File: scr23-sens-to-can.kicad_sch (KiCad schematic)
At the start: 61 parts, among them IC1 ADS1256IDBRG4, J1 ATM13-12PA-BM01, J2 6473711-1, J3 Conn_ST_STDC14, SW1 SW_SPDT, U1 SRV05-4, U10 AP63205WU, U2 SRV05-4, U4 TJA1042T-3, U5 AP7370-33Y-13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

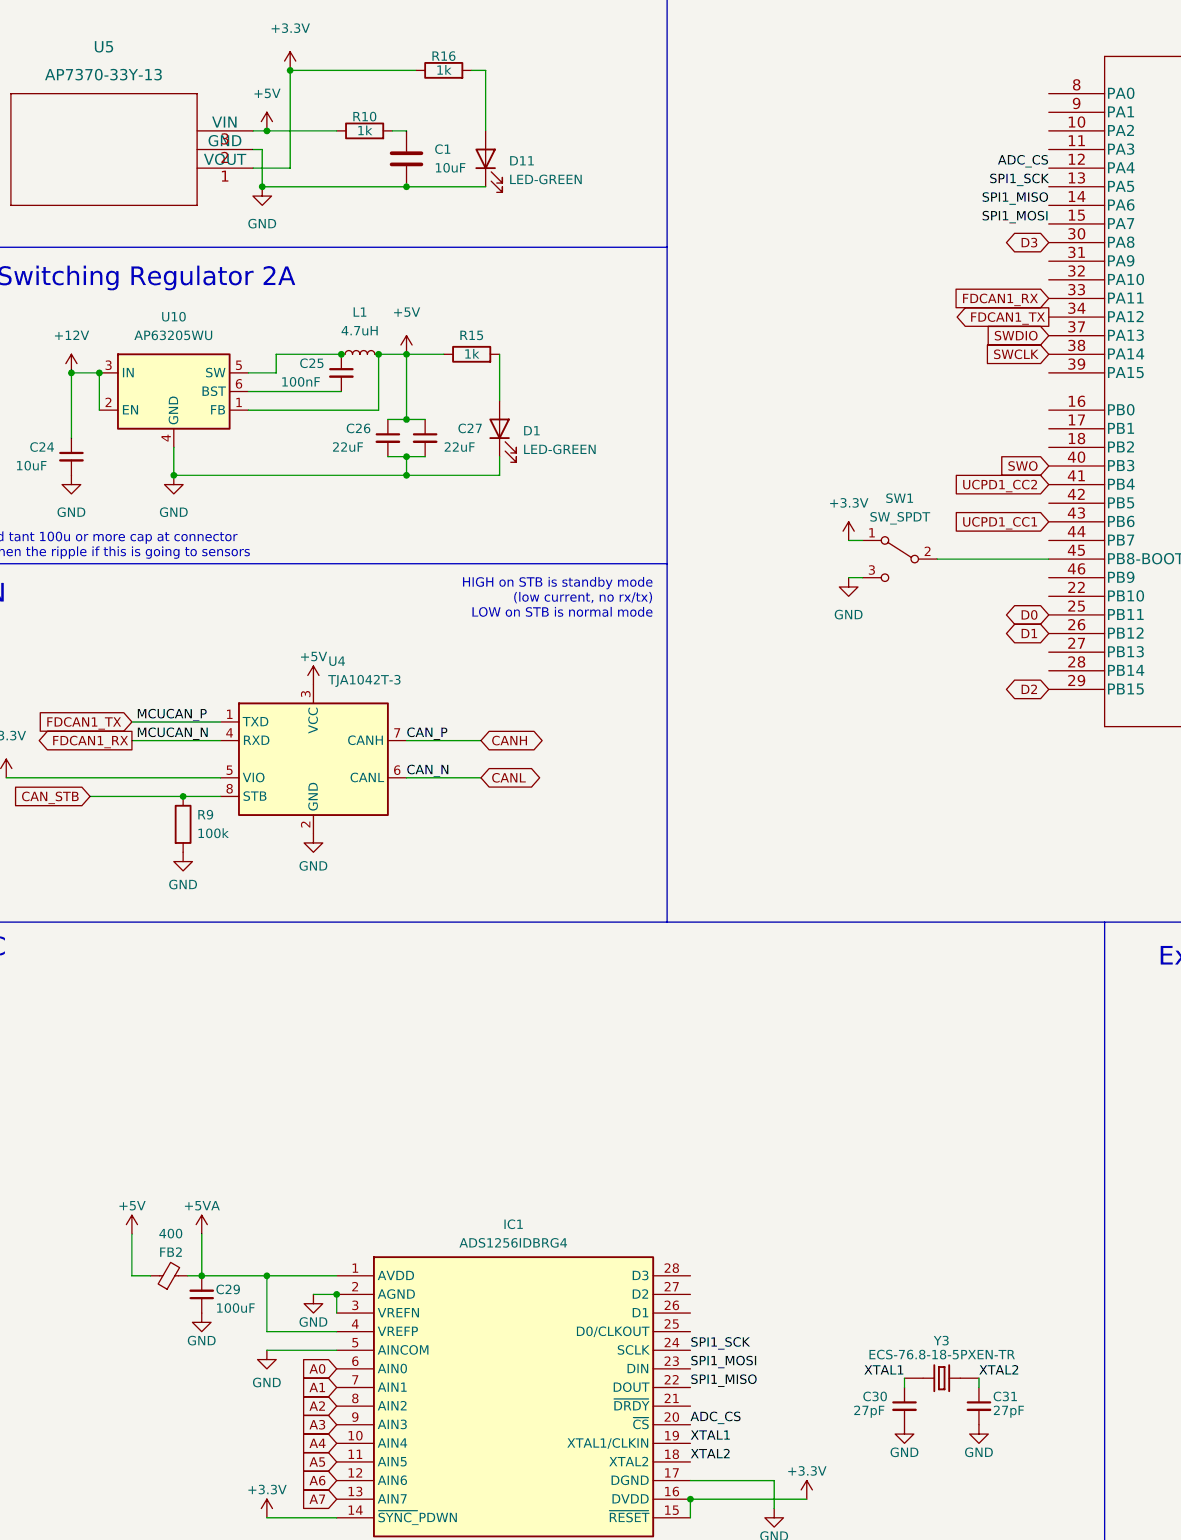
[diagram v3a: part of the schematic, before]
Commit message: add voltage reference, might need to change switching regulator cap packages
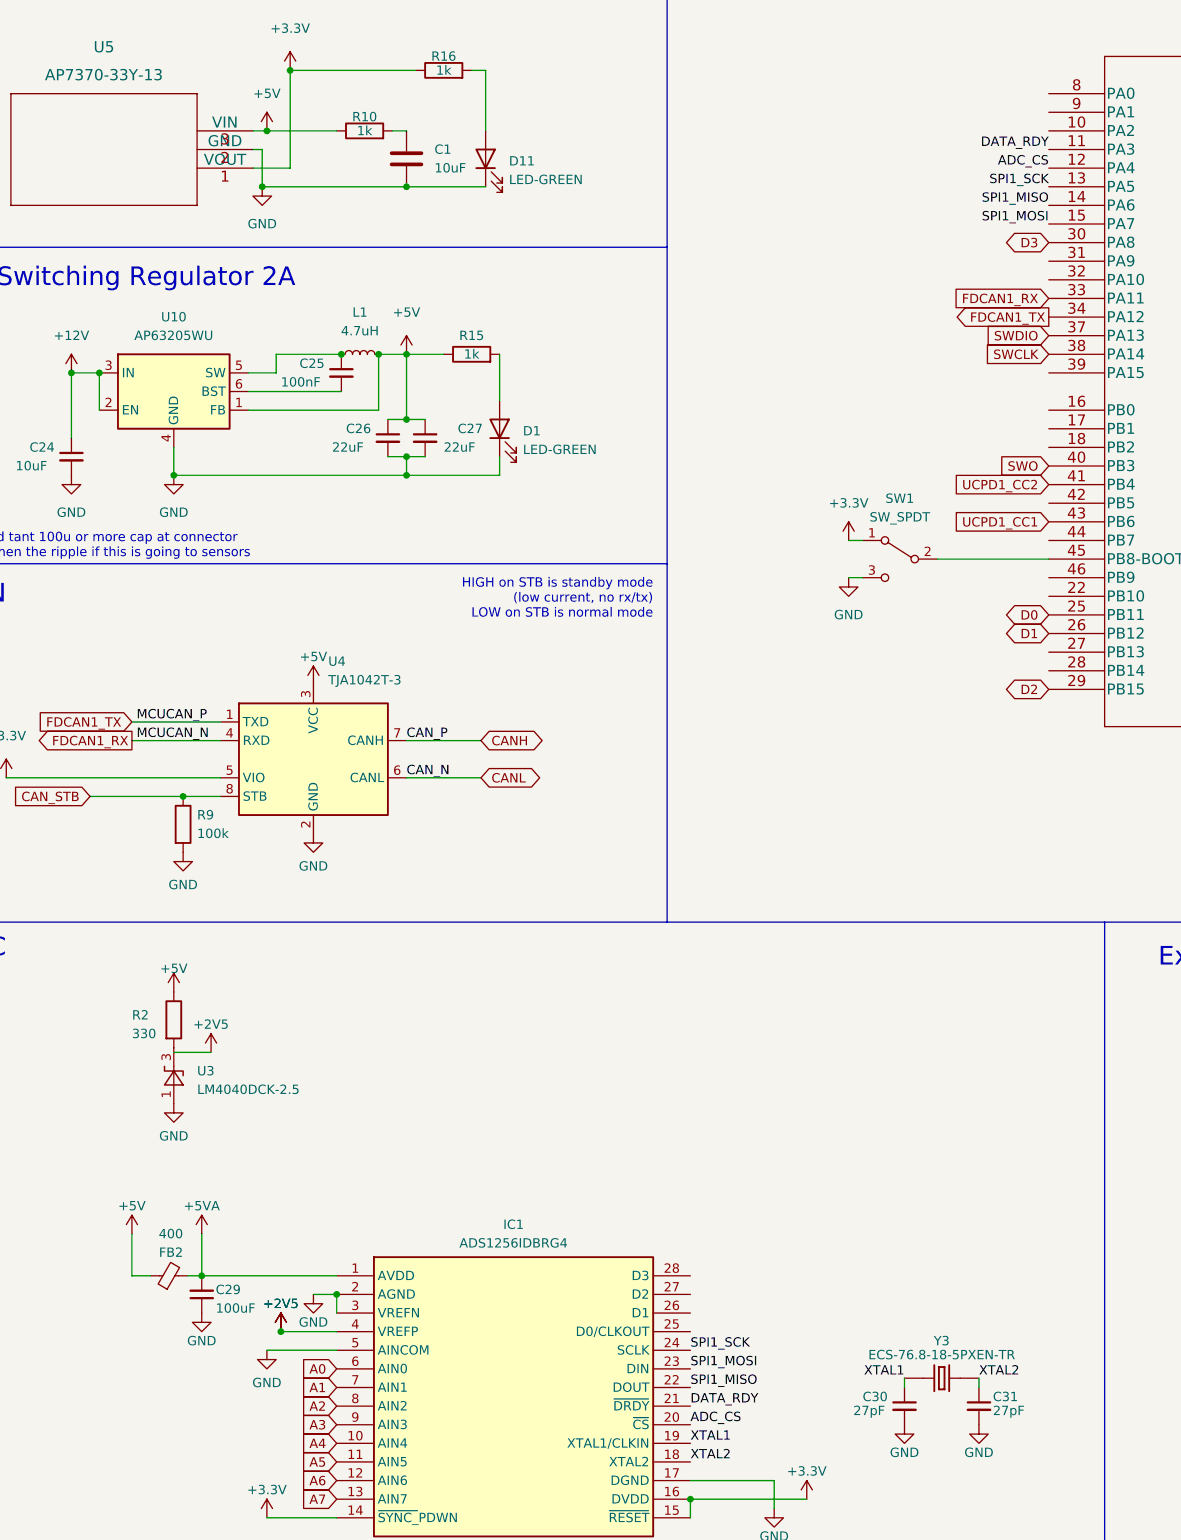
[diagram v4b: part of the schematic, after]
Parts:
- added R2: 330, Resistor_SMD:R_0603_1608Metric, symbol Device:R
- added U3: LM4040DCK-2.5, Package_TO_SOT_SMD:SOT-353_SC-70-5, symbol Reference_Voltage:LM4040DCK-2.5
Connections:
- net +5V: now also R2.1
- net +5VA: no longer IC1.4 (VREFP)
- net GND: now also U3.1 (A)
- net DATA_RDY: now reaches IC1.21 (~{DRDY})
- net DATA_RDY: now also U8.11 (PA3)
- new net: R2.2, U3.3 (K)
- new net +2V5: IC1.4 (VREFP)
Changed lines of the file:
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@@
   (junction (at 371.475 182.88) (diameter 0) (color 0 0 0 0)
   )
-  (junction (at 155.575 195.58) (diameter 0) (color 0 0 0 0)
-  )
   (junction (at 320.675 182.88) (diameter 0) (color 0 0 0 0)
   )
@@
   (junction (at 165.1 198.12) (diameter 0) (color 0 0 0 0)
   )
+  (junction (at 157.48 203.2) (diameter 0) (color 0 0 0 0)
+  )
   (junction (at 213.36 226.06) (diameter 0) (color 0 0 0 0)
   )
@@
     (stroke (width 0) (type default))
   )
+  (wire (pts (xy 142.875 165.1) (xy 147.955 165.1))
+    (stroke (width 0) (type default))
+  )
   (wire (pts (xy 361.95 123.825) (xy 368.935 123.825))
     (stroke (width 0) (type default))
@@
     (stroke (width 0) (type default))
   )
-  (wire (pts (xy 165.1 203.2) (xy 155.575 203.2))
-    (stroke (width 0) (type default))
-  )
   (wire (pts (xy 31.75 174.625) (xy 31.75 177.165))
     (stroke (width 0) (type default))
@@
     (stroke (width 0) (type default))
   )
+  (wire (pts (xy 157.48 203.2) (xy 165.1 203.2))
+    (stroke (width 0) (type default))
+  )
   (wire (pts (xy 128.905 72.39) (xy 128.905 81.28))
     (stroke (width 0) (type default))
@@
     (stroke (width 0) (type default))
   )
-  (wire (pts (xy 146.685 195.58) (xy 155.575 195.58))
-    (stroke (width 0) (type default))
-  )
-  (wire (pts (xy 155.575 195.58) (xy 155.575 203.2))
-    (stroke (width 0) (type default))
-  )
   (wire (pts (xy 213.36 226.06) (xy 229.235 226.06))
     (stroke (width 0) (type default))
@@
     (stroke (width 0) (type default))
   )
-  (wire (pts (xy 155.575 195.58) (xy 165.1 195.58))
+  (wire (pts (xy 146.685 195.58) (xy 165.1 195.58))
     (stroke (width 0) (type default))
   )
@@
     (effects (font (size 1.27 1.27)) (justify right bottom))
   )
+  (label "DATA_RDY" (at 213.36 213.36 0) (fields_autoplaced)
+    (effects (font (size 1.27 1.27)) (justify left bottom))
+  )
   (label "NRST" (at 369.57 76.2 0) (fields_autoplaced)
     (effects (font (size 1.27 1.27)) (justify left bottom))
@@
     (effects (font (size 1.27 1.27)) (justify left bottom))
   )
+  (label "DATA_RDY" (at 262.255 41.91 180) (fields_autoplaced)
+    (effects (font (size 1.27 1.27)) (justify right bottom))
+  )
   (label "XTAL2" (at 213.36 220.98 0) (fields_autoplaced)
     (effects (font (size 1.27 1.27)) (justify left bottom))
@@
     )
   )
+  (symbol (lib_id "power:+2V5") (at 147.955 165.1 0) (unit 1)
+    (in_bom yes) (on_board yes) (dnp no) (fields_autoplaced)
+    (property "Reference" "#PWR041" (at 147.955 168.91 0)
+      (effects (font (size 1.27 1.27)) hide)
+    )
+    (property "Value" "+2V5" (at 147.955 161.29 0)
+      (effects (font (size 1.27 1.27)))
+    )
+    (property "Footprint" "" (at 147.955 165.1 0)
+      (effects (font (size 1.27 1.27)) hide)
+    )
+    (property "Datasheet" "" (at 147.955 165.1 0)
+      (effects (font (size 1.27 1.27)) hide)
+    )
+    (pin "1")
+    (instances
+      (project "scr23-sens-to-can"
+        (path "/9d4a62b8-9a16-4c8d-8b16-7072bfb3ee3d"
+          (reference "#PWR041") (unit 1)
+        )
+      )
+    )
+  )
   (symbol (lib_id "Device:C") (at 355.6 60.96 90) (unit 1)
     (in_bom no) (on_board no) (dnp yes)
@@
     )
   )
+  (symbol (lib_id "power:+2V5") (at 157.48 203.2 0) (unit 1)
+    (in_bom yes) (on_board yes) (dnp no) (fields_autoplaced)
+    (property "Reference" "#PWR053" (at 157.48 207.01 0)
+      (effects (font (size 1.27 1.27)) hide)
+    )
+    (property "Value" "+2V5" (at 157.48 199.39 0)
+      (effects (font (size 1.27 1.27)))
+    )
+    (property "Footprint" "" (at 157.48 203.2 0)
+      (effects (font (size 1.27 1.27)) hide)
+    )
+    (property "Datasheet" "" (at 157.48 203.2 0)
+      (effects (font (size 1.27 1.27)) hide)
+    )
+    (pin "1")
+    (instances
+      (project "scr23-sens-to-can"
+        (path "/9d4a62b8-9a16-4c8d-8b16-7072bfb3ee3d"
+          (reference "#PWR053") (unit 1)
+        )
+      )
+    )
+  )
   (symbol (lib_id "Device:C") (at 361.315 179.07 180) (unit 1)
     (in_bom yes) (on_board yes) (dnp no) (fields_autoplaced)
@@
     )
   )
+  (symbol (lib_id "Reference_Voltage:LM4040DCK-2.5") (at 142.875 168.275 90) (unit 1)
+    (in_bom yes) (on_board yes) (dnp no) (fields_autoplaced)
+    (property "Reference" "U3" (at 146.05 167.64 90)
+      (effects (font (size 1.27 1.27)) (justify right))
+    )
+    (property "Value" "LM4040DCK-2.5" (at 146.05 170.18 90)
+      (effects (font (size 1.27 1.27)) (justify right))
+    )
+    (property "Footprint" "Package_TO_SOT_SMD:SOT-353_SC-70-5" (at 147.955 168.275 0)
+      (effects (font (size 1.27 1.27) italic) hide)
+    )
+    (property "Datasheet" "http://www.ti.com/lit/ds/symlink/lm4040-n.pdf" (at 142.875 168.275 0)
+      (effects (font (size 1.27 1.27) italic) hide)
+    )
+    (pin "1")
+    (pin "3")
+    (instances
+      (project "scr23-sens-to-can"
+        (path "/9d4a62b8-9a16-4c8d-8b16-7072bfb3ee3d"
+          (reference "U3") (unit 1)
+        )
+      )
+    )
+  )
   (symbol (lib_id "power:+5VA") (at 146.685 189.865 0) (unit 1)
     (in_bom yes) (on_board yes) (dnp no)
@@
     )
   )
+  (symbol (lib_name "+5V_2") (lib_id "power:+5V") (at 142.875 156.845 0) (unit 1)
+    (in_bom yes) (on_board yes) (dnp no) (fields_autoplaced)
+    (property "Reference" "#PWR042" (at 142.875 160.655 0)
+      (effects (font (size 1.27 1.27)) hide)
+    )
+    (property "Value" "+5V" (at 142.875 153.67 0)
+      (effects (font (size 1.27 1.27)))
+    )
+    (property "Footprint" "" (at 142.875 156.845 0)
+      (effects (font (size 1.27 1.27)) hide)
+    )
+    (property "Datasheet" "" (at 142.875 156.845 0)
+      (effects (font (size 1.27 1.27)) hide)
+    )
+    (pin "1")
+    (instances
+      (project "scr23-sens-to-can"
+        (path "/9d4a62b8-9a16-4c8d-8b16-7072bfb3ee3d"
+          (reference "#PWR042") (unit 1)
+        )
+      )
+    )
+  )
   (symbol (lib_id "Device:C") (at 382.27 200.025 180) (unit 1)
     (in_bom yes) (on_board yes) (dnp no) (fields_autoplaced)
@@
     )
   )
+  (symbol (lib_name "GND_6") (lib_id "power:GND") (at 142.875 172.085 0) (unit 1)
+    (in_bom yes) (on_board yes) (dnp no) (fields_autoplaced)
+    (property "Reference" "#PWR052" (at 142.875 178.435 0)
+      (effects (font (size 1.27 1.27)) hide)
+    )
+    (property "Value" "GND" (at 142.875 176.53 0)
+      (effects (font (size 1.27 1.27)))
+    )
+    (property "Footprint" "" (at 142.875 172.085 0)
+      (effects (font (size 1.27 1.27)) hide)
+    )
+    (property "Datasheet" "" (at 142.875 172.085 0)
+      (effects (font (size 1.27 1.27)) hide)
+    )
+    (pin "1")
+    (instances
+      (project "scr23-sens-to-can"
+        (path "/9d4a62b8-9a16-4c8d-8b16-7072bfb3ee3d"
+          (reference "#PWR052") (unit 1)
+        )
+      )
+    )
+  )
   (symbol (lib_id "Device:C") (at 391.795 200.025 180) (unit 1)
     (in_bom yes) (on_board yes) (dnp no) (fields_autoplaced)
@@
     )
   )
+  (symbol (lib_id "Device:R") (at 142.875 160.655 0) (unit 1)
+    (in_bom yes) (on_board yes) (dnp no)
+    (property "Reference" "R2" (at 137.16 160.02 0)
+      (effects (font (size 1.27 1.27)) (justify left))
+    )
+    (property "Value" "330" (at 137.16 162.56 0)
+      (effects (font (size 1.27 1.27)) (justify left))
+    )
+    (property "Footprint" "Resistor_SMD:R_0603_1608Metric" (at 141.097 160.655 90)
+      (effects (font (size 1.27 1.27)) hide)
+    )
+    (property "Datasheet" "~" (at 142.875 160.655 0)
+      (effects (font (size 1.27 1.27)) hide)
+    )
+    (pin "1")
+    (pin "2")
+    (instances
+      (project "scr23-sens-to-can"
+        (path "/9d4a62b8-9a16-4c8d-8b16-7072bfb3ee3d"
+          (reference "R2") (unit 1)
+        )
+      )
+    )
+  )
   (symbol (lib_id "Device:C_Small") (at 128.905 83.82 0) (unit 1)
     (in_bom yes) (on_board yes) (dnp no)
@@
         )
       )
+    )
+  )
+  (symbol (lib_id "power:+2V5") (at 157.48 203.2 0) (unit 1)
+    (in_bom yes) (on_board yes) (dnp no) (fields_autoplaced)
+    (property "Reference" "#PWR054" (at 157.48 207.01 0)
+      (effects (font (size 1.27 1.27)) hide)
+    )
+    (property "Value" "+2V5" (at 157.48 199.39 0)
+      (effects (font (size 1.27 1.27)))
+    )
+    (property "Footprint" "" (at 157.48 203.2 0)
+      (effects (font (size 1.27 1.27)) hide)
+    )
+    (property "Datasheet" "" (at 157.48 203.2 0)
+      (effects (font (size 1.27 1.27)) hide)
+    )
+    (pin "1")
+    (instances
+      (project "scr23-sens-to-can"
+        (path "/9d4a62b8-9a16-4c8d-8b16-7072bfb3ee3d"
+          (reference "#PWR054") (unit 1)
+        )
+      )
